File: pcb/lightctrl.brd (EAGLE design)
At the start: 46.4 x 34.3 mm, 30 parts, among them IC1 AtMega644A/1284, K1 AQY2212VEHA, Q1 3.6864MHz, X1 ISP/UART

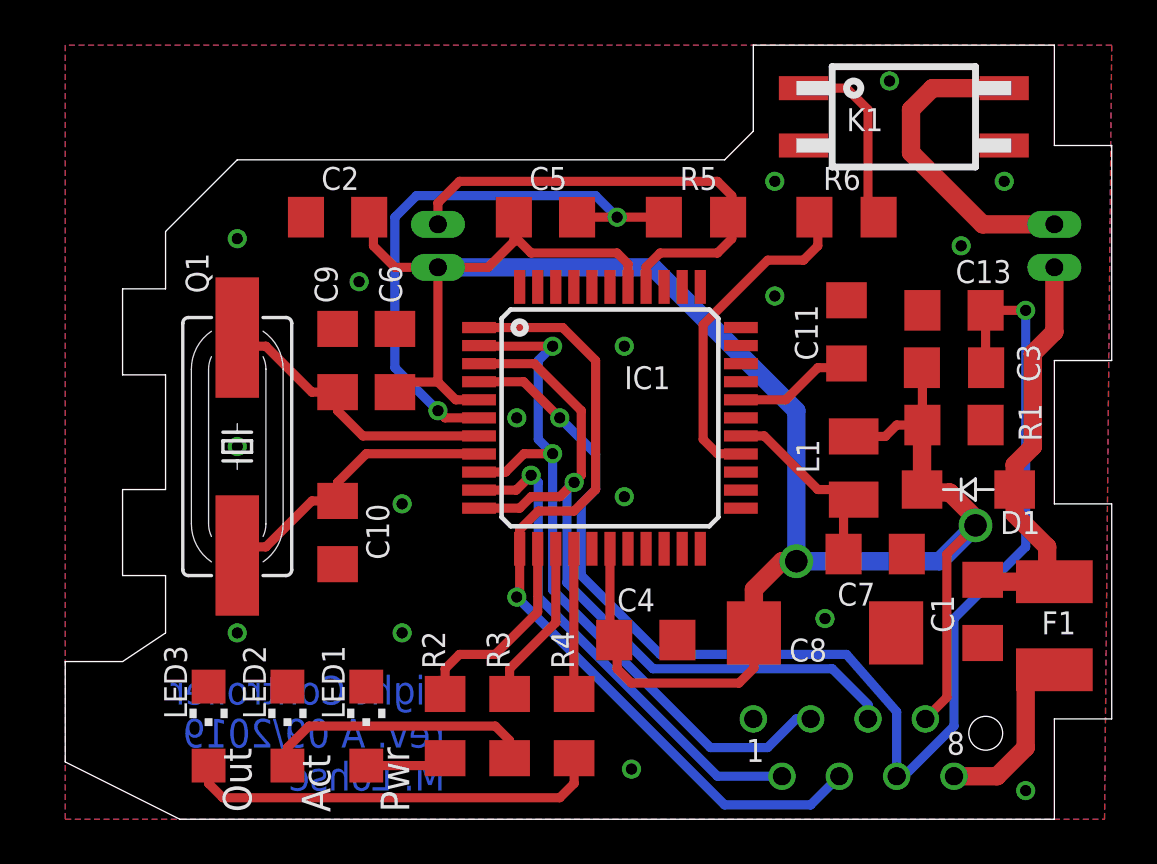
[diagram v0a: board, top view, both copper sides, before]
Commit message: Update pcb and documentation to rev.B: fix padsize for D1, add gpio protection for MCU, slightly widen board to get better grip in battery compartment
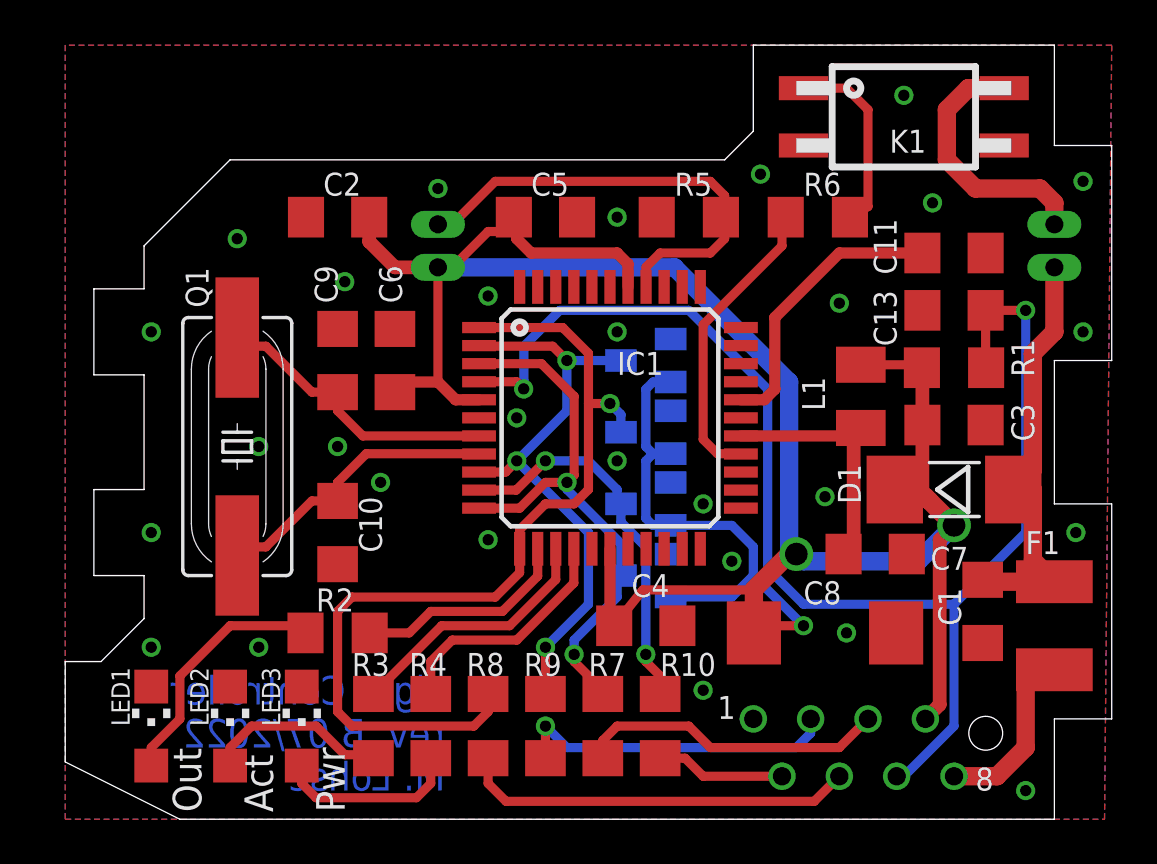
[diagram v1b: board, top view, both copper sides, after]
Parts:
- added D2, D3, D4, D5: BAS40-04, diode:SOT23
- added R10, R7, R8, R9: 1k, rcl:R1206
- D1: device diode:SMA-DO214AC -> diode:MELF-MLL41
- moved LED1 9.53 mm to (3.81, 4.13)
- moved R4 6.35 mm to (16.2, 4.13)
- moved R2 6.30 mm to (12.1, 8.26), turned to 0 degrees
- moved R3 6.03 mm to (13.7, 4.13)
- moved C11 5.91 mm to (39.4, 25.1), turned to 0 degrees
- moved LED3 4.13 mm to (10.5, 4.13)
- moved L1 3.19 mm to (35.2, 18.7)
- moved LED2 2.54 mm to (7.30, 4.13)
- moved R6 1.27 mm to (33.3, 26.7)
- moved D1 0.64 mm to (39.4, 14.6), turned to 0 degrees
- moved C4 0.63 mm to (25.7, 8.57)
- moved R5 0.32 mm to (27.6, 26.7)
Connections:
- new net N$13: R7.2, X1.5
- new net N$15: R8.2, X1.4
- new net N$16: R9.2, X1.3
- new net N$18: R10.2, X1.2
- net GND: now also D2.1, D3.1, D4.1, D5.1
- net RX0/MISO: now also D2.3, R9.1; no longer X1.3
- net RX1/SCK: now also D4.3, R7.1; no longer X1.5
- net TX0: now also D5.3, R10.1; no longer X1.2
- net TX1/MOSI: now also D3.3, R8.1; no longer X1.4
- net VCC: now also D1.C, D2.2, D3.2, D4.2, D5.2; no longer D1.K
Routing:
- net GND: track 25.8 -> 0.00 mm, vias 19 -> 29
- net VCC: track 99.7 -> 122.7 mm, vias 2 -> 3
- net N$15: track 0.00 -> 17.5 mm
- net N$16: track 0.00 -> 14.5 mm, vias 0 -> 1
- net N$13: track 0.00 -> 13.7 mm
- net N$9: track 18.6 -> 8.15 mm
- net RX1/SCK: track 34.2 -> 24.9 mm, vias 1 -> 2
- net N$7: track 3.63 -> 11.1 mm
- net N$3: track 5.34 -> 12.6 mm
- net N$18: track 0.00 -> 5.73 mm
- net RX0/MISO: track 33.0 -> 27.7 mm, vias 2 -> 3
- net TX0: track 22.2 -> 17.0 mm, vias 1 -> 2
- net N$12: track 6.44 -> 10.7 mm
- net N$11: track 7.28 -> 11.5 mm
- net N$8: track 12.1 -> 8.13 mm
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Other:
- outline, holes or cut-outs redrawn
- board text added: "1 GND 2 TX0 3 RX0/MISO 4 TX1/MOSI 5 RX1/SCK 6 RESET 7 VCC/VTG 8 VDD (5V)"
- board text added: "ISP/UART"
- board text added: "Light Controller rev. B 07/2022 M. Lohse"
- board text removed: "ISP/UART 1 GND 2 TX0 3 RX0/MISO 4 TX1/MOSI 5 RX1/SCK 6 RESET 7 VCC/VTG 8 VDD (5V)"
- board text removed: "Light Controller rev. A 09/2019 M. Lohse"
